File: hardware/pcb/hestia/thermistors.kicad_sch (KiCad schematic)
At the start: 60 parts, among them J10 Conn_01x02_Female, J11 Conn_01x02_Female, J12 Conn_01x02_Female, J13 Conn_01x02_Female, J14 Conn_01x02_Female, J15 Conn_01x02_Female, J16 Conn_01x02_Female, J7 Conn_01x02_Female, J8 Conn_01x02_Female, J9 Conn_01x02_Female, U4 MAX31725MTA+T, U5 MAX31725MTA+T, U6 MAX31725MTA+T, U7 MAX31725MTA+T

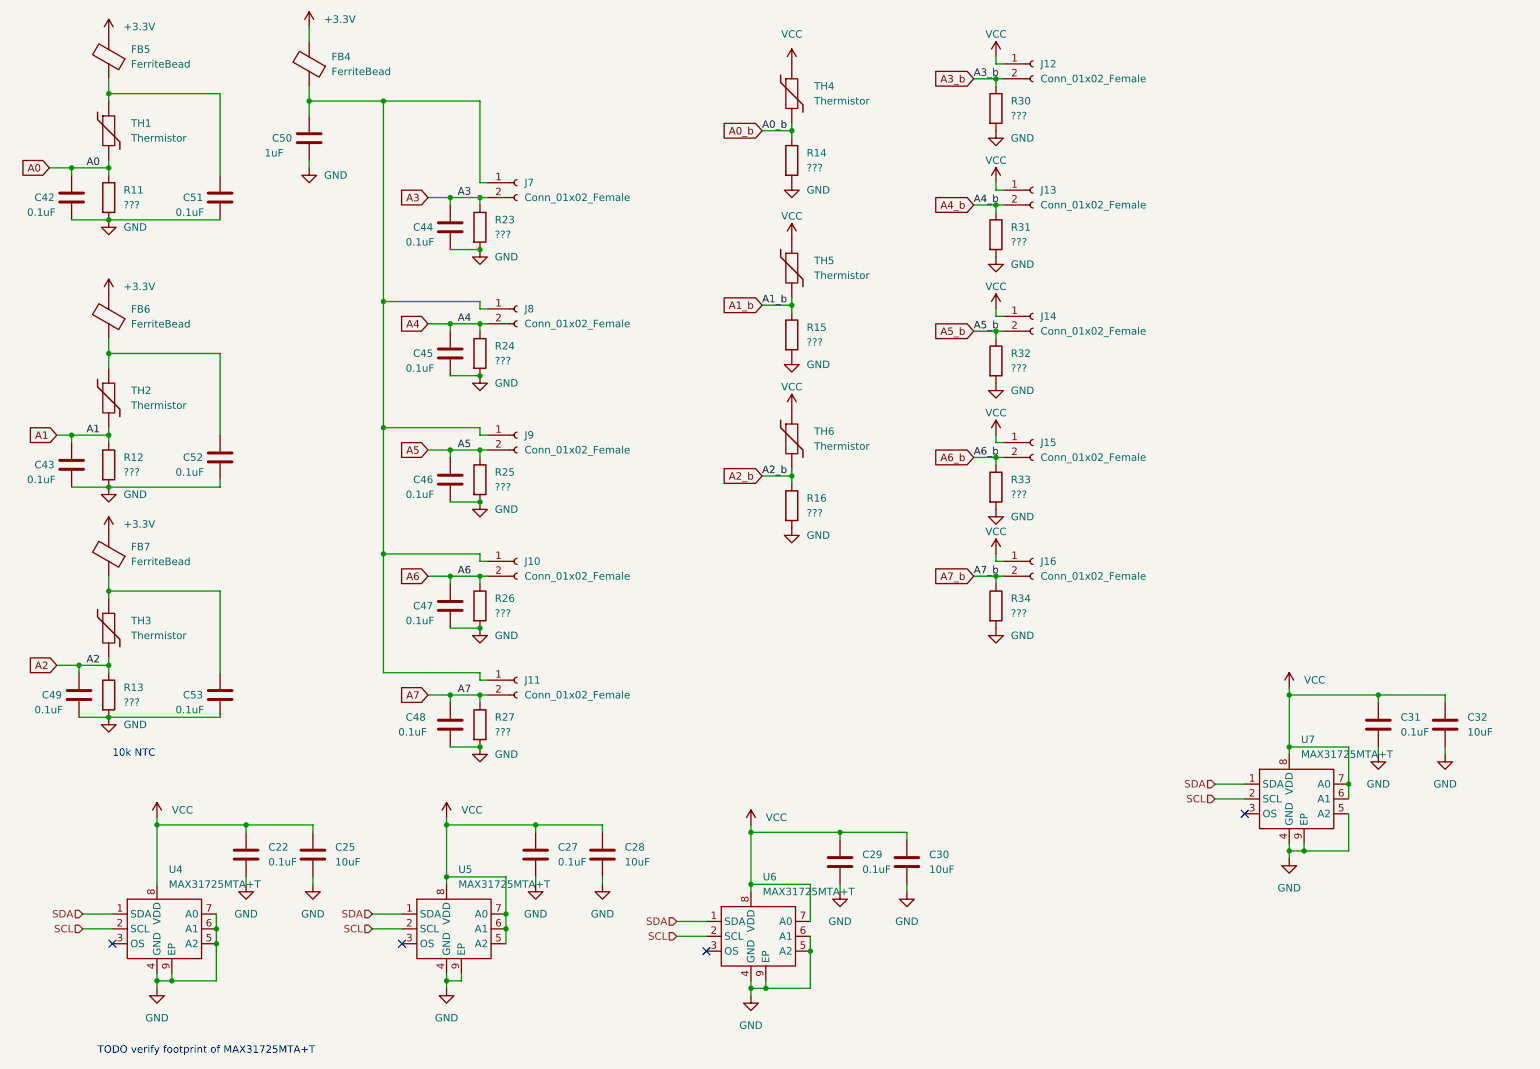
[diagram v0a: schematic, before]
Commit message: edit some component values
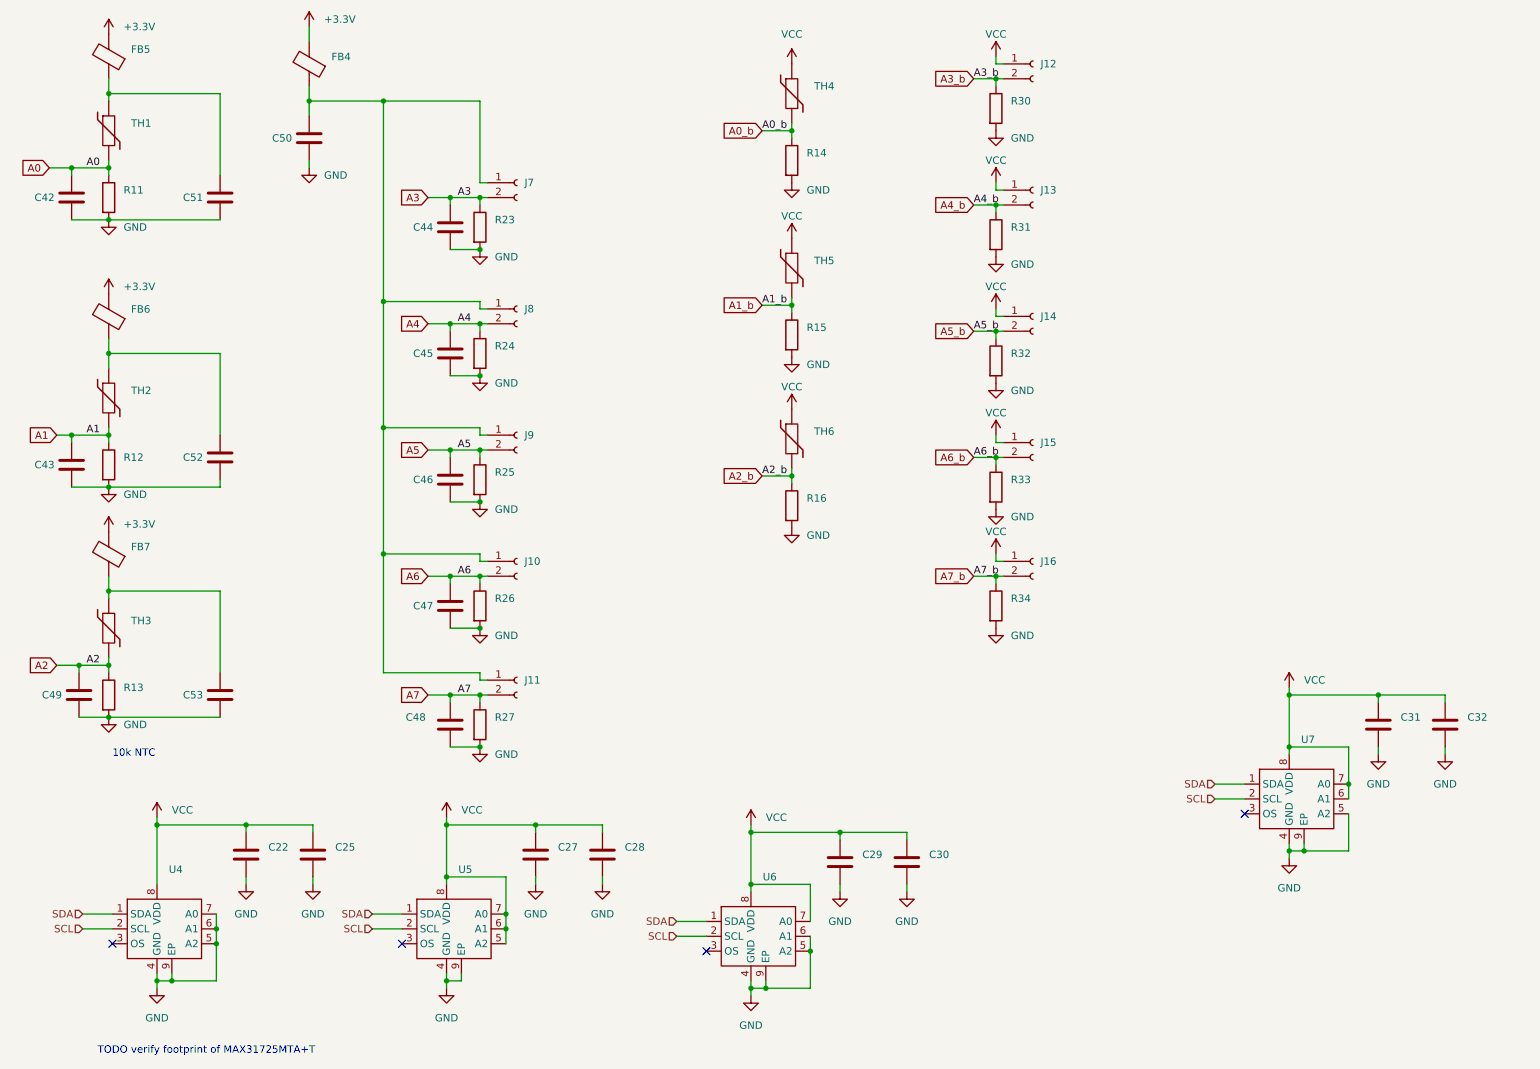
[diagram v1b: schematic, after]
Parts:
- C22, C27, C29, C31, C42, C43, C44, C45, C46, C47, C48, C49, C51, C52, C53: value 0.1uF -> (none); footprint Capacitor_SMD:C_0603_1608Metric_Pad1.08x0.95mm_HandSolder -> (none)
- C25, C28, C30, C32: value 10uF -> (none); footprint Capacitor_SMD:C_0603_1608Metric_Pad1.08x0.95mm_HandSolder -> (none)
- C50: value 1uF -> (none); footprint Capacitor_SMD:C_0603_1608Metric_Pad1.08x0.95mm_HandSolder -> (none)
- FB4, FB5, FB6, FB7: value FerriteBead -> (none); footprint Resistor_SMD:R_0603_1608Metric_Pad0.98x0.95mm_HandSolder -> (none)
- J10, J11, J12, J13, J14, J15, J16, J7, J8, J9: value Conn_01x02_Female -> (none); footprint Connector_PinHeader_1.27mm:PinHeader_1x02_P1.27mm_Vertical -> (none)
- R11, R12, R13, R14, R15, R16, R23, R24, R25, R26, R27, R30, R31, R32, R33, R34: value ??? -> (none); footprint Resistor_SMD:R_0603_1608Metric_Pad0.98x0.95mm_HandSolder -> (none)
- TH1, TH2, TH3, TH4, TH5, TH6: value Thermistor -> (none); footprint Resistor_SMD:R_0603_1608Metric_Pad0.98x0.95mm_HandSolder -> (none)
- U4, U5, U6, U7: value MAX31725MTA+T -> (none); footprint Package_DFN_QFN:DFN-8-1EP_3x3mm_P0.65mm_EP1.55x2.4mm -> (none)

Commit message: Terminate pin 12 (LDR) on LM2655 to fix ERC warning
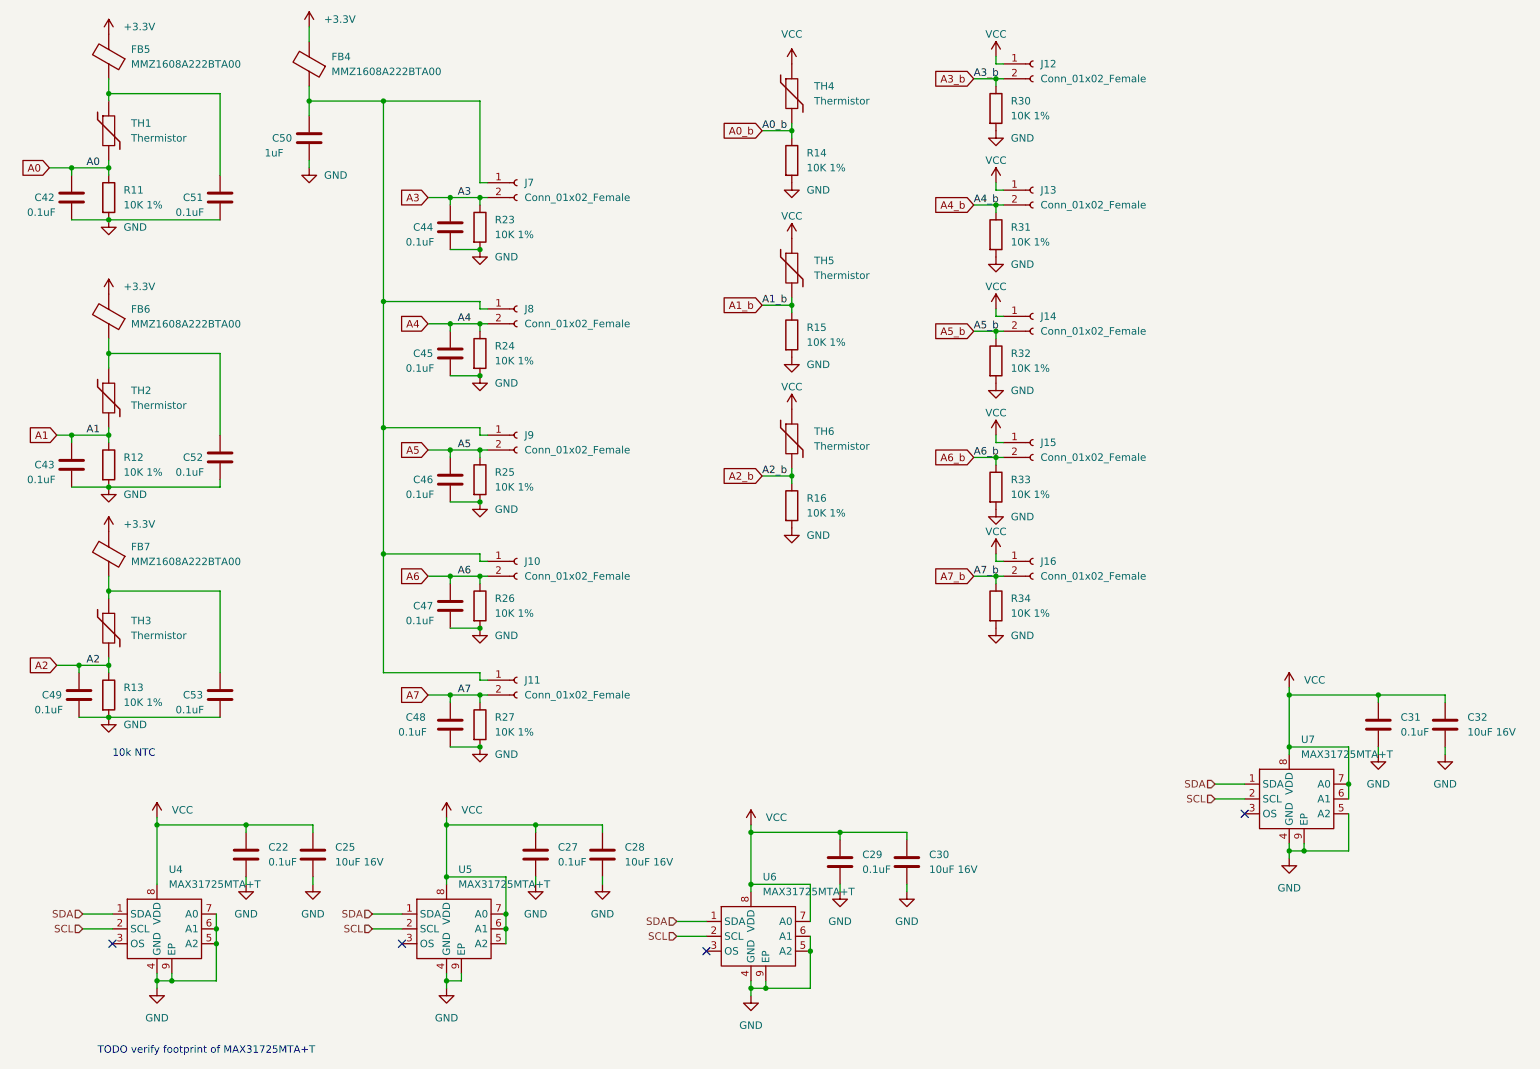
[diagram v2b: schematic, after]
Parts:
- C22, C27, C29, C31, C42, C43, C44, C45, C46, C47, C48, C49, C51, C52, C53: value (none) -> 0.1uF; footprint (none) -> Capacitor_SMD:C_0603_1608Metric_Pad1.08x0.95mm_HandSolder
- C25, C28, C30, C32: value (none) -> 10uF 16V; footprint (none) -> Capacitor_SMD:C_0603_1608Metric_Pad1.08x0.95mm_HandSolder
- C50: value (none) -> 1uF; footprint (none) -> Capacitor_SMD:C_0603_1608Metric_Pad1.08x0.95mm_HandSolder
- FB4, FB5, FB6, FB7: value (none) -> MMZ1608A222BTA00; footprint (none) -> Resistor_SMD:R_0603_1608Metric_Pad0.98x0.95mm_HandSolder
- J10, J11, J12, J13, J14, J15, J16, J7, J8, J9: value (none) -> Conn_01x02_Female; footprint (none) -> Connector_PinHeader_1.27mm:PinHeader_1x02_P1.27mm_Vertical
- R11, R12, R13, R14, R15, R16, R23, R24, R25, R26, R27, R30, R31, R32, R33, R34: value (none) -> 10K 1%; footprint (none) -> Resistor_SMD:R_0603_1608Metric_Pad0.98x0.95mm_HandSolder
- TH1, TH2, TH3, TH4, TH5, TH6: value (none) -> Thermistor; footprint (none) -> Resistor_SMD:R_0603_1608Metric_Pad0.98x0.95mm_HandSolder
- U4, U5, U6, U7: value (none) -> MAX31725MTA+T; footprint (none) -> Package_DFN_QFN:DFN-8-1EP_3x3mm_P0.65mm_EP1.55x2.4mm

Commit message: Bump version to 2.0, add title to all schematic pages
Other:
- company: (none) -> Mawson Rovers
- title: (none) -> Hestia
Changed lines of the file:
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@@
 (kicad_sch (version 20211123) (generator eeschema)
   (paper "A4")
+  (title_block
+    (title "Hestia")
+    (date "2022-07-14")
+    (rev "2.0")
+    (company "Mawson Rovers")
+  )
   (junction (at 234.315 139.7) (diameter 0) (color 0 0 0 0)
   )

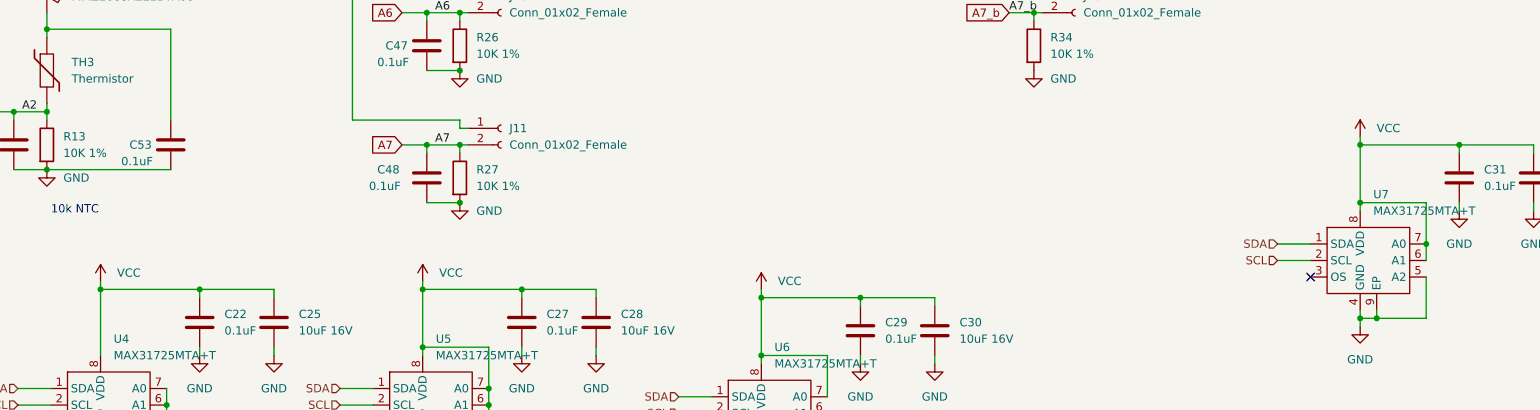
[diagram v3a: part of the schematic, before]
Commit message: updater thermistor to 3.3v supply
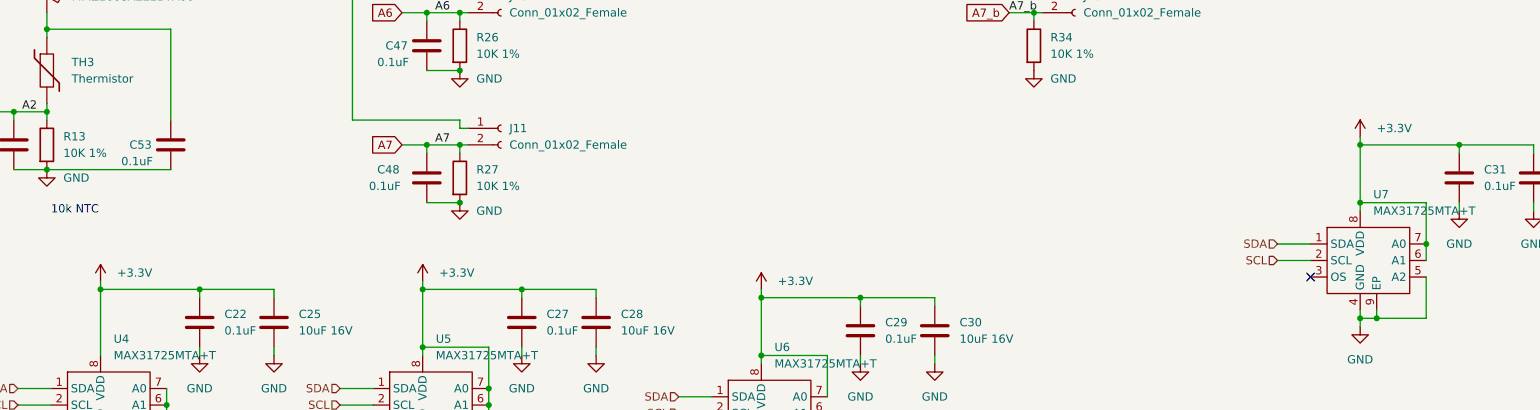
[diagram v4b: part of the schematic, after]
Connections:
- net +3V3: now also C22.1, C25.1, C27.1, C28.1, C29.1, C30.1, C31.1, C32.1, U4.8 (VDD), U5.5 (A2), U5.6 (A1), U5.7 (A0), U5.8 (VDD), U6.7 (A0), U6.8 (VDD), U7.6 (A1), U7.7 (A0), U7.8 (VDD)
- net VCC: no longer C22.1, C25.1, C27.1, C28.1, C29.1, C30.1, C31.1, C32.1, U4.8 (VDD), U5.5 (A2), U5.6 (A1), U5.7 (A0), U5.8 (VDD), U6.7 (A0), U6.8 (VDD), U7.6 (A1), U7.7 (A0), U7.8 (VDD)
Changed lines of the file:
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@@
     (pin "2")
+  )
+  (symbol (lib_id "power:+3.3V") (at 40.64 151.765 0) (unit 1)
+    (in_bom yes) (on_board yes) (fields_autoplaced)
+    (property "Reference" "#PWR?" (id 0) (at 40.64 155.575 0)
+      (effects (font (size 1.27 1.27)) hide)
+    )
+    (property "Value" "+3.3V" (id 1) (at 43.18 150.4949 0)
+      (effects (font (size 1.27 1.27)) (justify left))
+    )
+    (property "Footprint" "" (id 2) (at 40.64 151.765 0)
+      (effects (font (size 1.27 1.27)) hide)
+    )
+    (property "Datasheet" "" (id 3) (at 40.64 151.765 0)
+      (effects (font (size 1.27 1.27)) hide)
+    )
+    (pin "1")
   )
   (symbol (lib_id "Device:C") (at 51.435 130.81 0) (unit 1)
@@
     )
     (property "Datasheet" "" (id 3) (at 32.385 62.23 0)
+      (effects (font (size 1.27 1.27)) hide)
+    )
+    (pin "1")
+  )
+  (symbol (lib_id "power:+3.3V") (at 142.24 153.035 0) (unit 1)
+    (in_bom yes) (on_board yes) (fields_autoplaced)
+    (property "Reference" "#PWR?" (id 0) (at 142.24 156.845 0)
+      (effects (font (size 1.27 1.27)) hide)
+    )
+    (property "Value" "+3.3V" (id 1) (at 144.78 151.7649 0)
+      (effects (font (size 1.27 1.27)) (justify left))
+    )
+    (property "Footprint" "" (id 2) (at 142.24 153.035 0)
+      (effects (font (size 1.27 1.27)) hide)
+    )
+    (property "Datasheet" "" (id 3) (at 142.24 153.035 0)
       (effects (font (size 1.27 1.27)) hide)
     )
@@
     (pin "9")
   )
+  (symbol (lib_id "power:+3.3V") (at 234.315 129.54 0) (unit 1)
+    (in_bom yes) (on_board yes) (fields_autoplaced)
+    (property "Reference" "#PWR?" (id 0) (at 234.315 133.35 0)
+      (effects (font (size 1.27 1.27)) hide)
+    )
+    (property "Value" "+3.3V" (id 1) (at 236.855 128.2699 0)
+      (effects (font (size 1.27 1.27)) (justify left))
+    )
+    (property "Footprint" "" (id 2) (at 234.315 129.54 0)
+      (effects (font (size 1.27 1.27)) hide)
+    )
+    (property "Datasheet" "" (id 3) (at 234.315 129.54 0)
+      (effects (font (size 1.27 1.27)) hide)
+    )
+    (pin "1")
+  )
   (symbol (lib_id "Device:C") (at 116.84 158.115 0) (unit 1)
     (in_bom yes) (on_board yes) (fields_autoplaced)
@@
     (pin "1")
   )
-  (symbol (lib_id "power:VCC") (at 40.64 151.765 0) (unit 1)
-    (in_bom yes) (on_board yes) (fields_autoplaced)
-    (property "Reference" "#PWR0151" (id 0) (at 40.64 155.575 0)
-      (effects (font (size 1.27 1.27)) hide)
-    )
-    (property "Value" "VCC" (id 1) (at 43.18 150.4949 0)
-      (effects (font (size 1.27 1.27)) (justify left))
-    )
-    (property "Footprint" "" (id 2) (at 40.64 151.765 0)
-      (effects (font (size 1.27 1.27)) hide)
-    )
-    (property "Datasheet" "" (id 3) (at 40.64 151.765 0)
-      (effects (font (size 1.27 1.27)) hide)
-    )
-    (pin "1")
-  )
   (symbol (lib_id "power:GND") (at 32.385 95.25 0) (unit 1)
     (in_bom yes) (on_board yes) (fields_autoplaced)
@@
     (pin "2")
   )
-  (symbol (lib_id "power:VCC") (at 142.24 153.035 0) (unit 1)
-    (in_bom yes) (on_board yes) (fields_autoplaced)
-    (property "Reference" "#PWR0145" (id 0) (at 142.24 156.845 0)
-      (effects (font (size 1.27 1.27)) hide)
-    )
-    (property "Value" "VCC" (id 1) (at 144.78 151.7649 0)
-      (effects (font (size 1.27 1.27)) (justify left))
-    )
-    (property "Footprint" "" (id 2) (at 142.24 153.035 0)
-      (effects (font (size 1.27 1.27)) hide)
-    )
-    (property "Datasheet" "" (id 3) (at 142.24 153.035 0)
-      (effects (font (size 1.27 1.27)) hide)
-    )
-    (pin "1")
-  )
   (symbol (lib_id "Device:R") (at 32.385 130.81 0) (unit 1)
     (in_bom yes) (on_board yes) (fields_autoplaced)
@@
     )
     (property "Datasheet" "" (id 3) (at 184.15 55.88 0)
+      (effects (font (size 1.27 1.27)) hide)
+    )
+    (pin "1")
+  )
+  (symbol (lib_id "power:+3.3V") (at 90.17 151.765 0) (unit 1)
+    (in_bom yes) (on_board yes) (fields_autoplaced)
+    (property "Reference" "#PWR?" (id 0) (at 90.17 155.575 0)
+      (effects (font (size 1.27 1.27)) hide)
+    )
+    (property "Value" "+3.3V" (id 1) (at 92.71 150.4949 0)
+      (effects (font (size 1.27 1.27)) (justify left))
+    )
+    (property "Footprint" "" (id 2) (at 90.17 151.765 0)
+      (effects (font (size 1.27 1.27)) hide)
+    )
+    (property "Datasheet" "" (id 3) (at 90.17 151.765 0)
       (effects (font (size 1.27 1.27)) hide)
     )
@@
     (pin "2")
   )
-  (symbol (lib_id "power:VCC") (at 234.315 129.54 0) (unit 1)
-    (in_bom yes) (on_board yes) (fields_autoplaced)
-    (property "Reference" "#PWR0163" (id 0) (at 234.315 133.35 0)
-      (effects (font (size 1.27 1.27)) hide)
-    )
-    (property "Value" "VCC" (id 1) (at 236.855 128.2699 0)
-      (effects (font (size 1.27 1.27)) (justify left))
-    )
-    (property "Footprint" "" (id 2) (at 234.315 129.54 0)
-      (effects (font (size 1.27 1.27)) hide)
-    )
-    (property "Datasheet" "" (id 3) (at 234.315 129.54 0)
-      (effects (font (size 1.27 1.27)) hide)
-    )
-    (pin "1")
-  )
   (symbol (lib_id "Device:C") (at 105.41 158.115 0) (unit 1)
     (in_bom yes) (on_board yes) (fields_autoplaced)
@@
       (effects (font (size 1.27 1.27)) hide)
     )
-    (pin "1")
-  )
-  (symbol (lib_id "power:VCC") (at 90.17 151.765 0) (unit 1)
-    (in_bom yes) (on_board yes) (fields_autoplaced)
-    (property "Reference" "#PWR0155" (id 0) (at 90.17 155.575 0)
-      (effects (font (size 1.27 1.27)) hide)
-    )
-    (property "Value" "VCC" (id 1) (at 92.71 150.4949 0)
-      (effects (font (size 1.27 1.27)) (justify left))
-    )
-    (property "Footprint" "" (id 2) (at 90.17 151.765 0)
-      (effects (font (size 1.27 1.27)) hide)
-    )
-    (property "Datasheet" "" (id 3) (at 90.17 151.765 0)
-      (effects (font (size 1.27 1.27)) hide)
-    )
